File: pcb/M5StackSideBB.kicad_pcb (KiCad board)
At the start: 2 copper layers, 100 x 50 mm, 15 parts, among them J1 Conn_01x14, J2 Conn_01x14, J3 Conn_02x15_Odd_Even, J4 Conn_02x15_Odd_Even

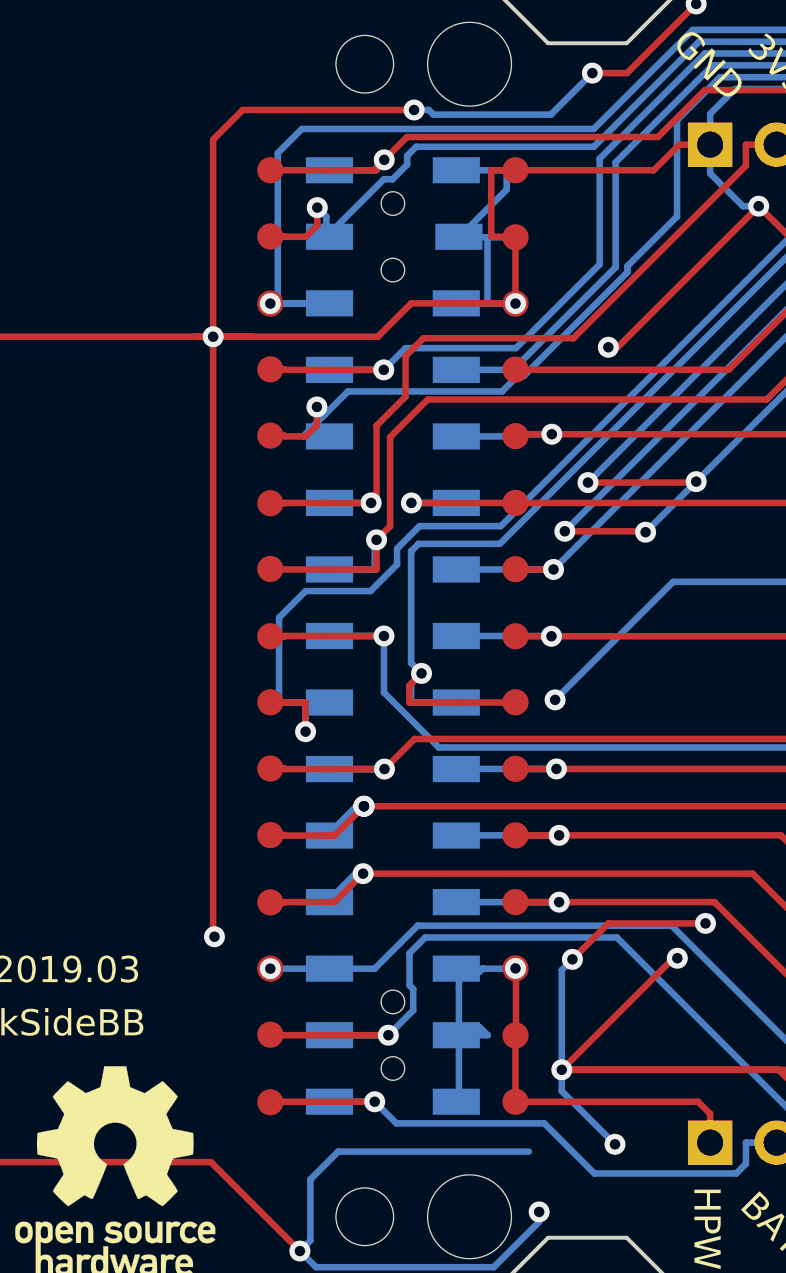
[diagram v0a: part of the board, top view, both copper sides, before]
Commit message: Add bottom pads for spacer PCB
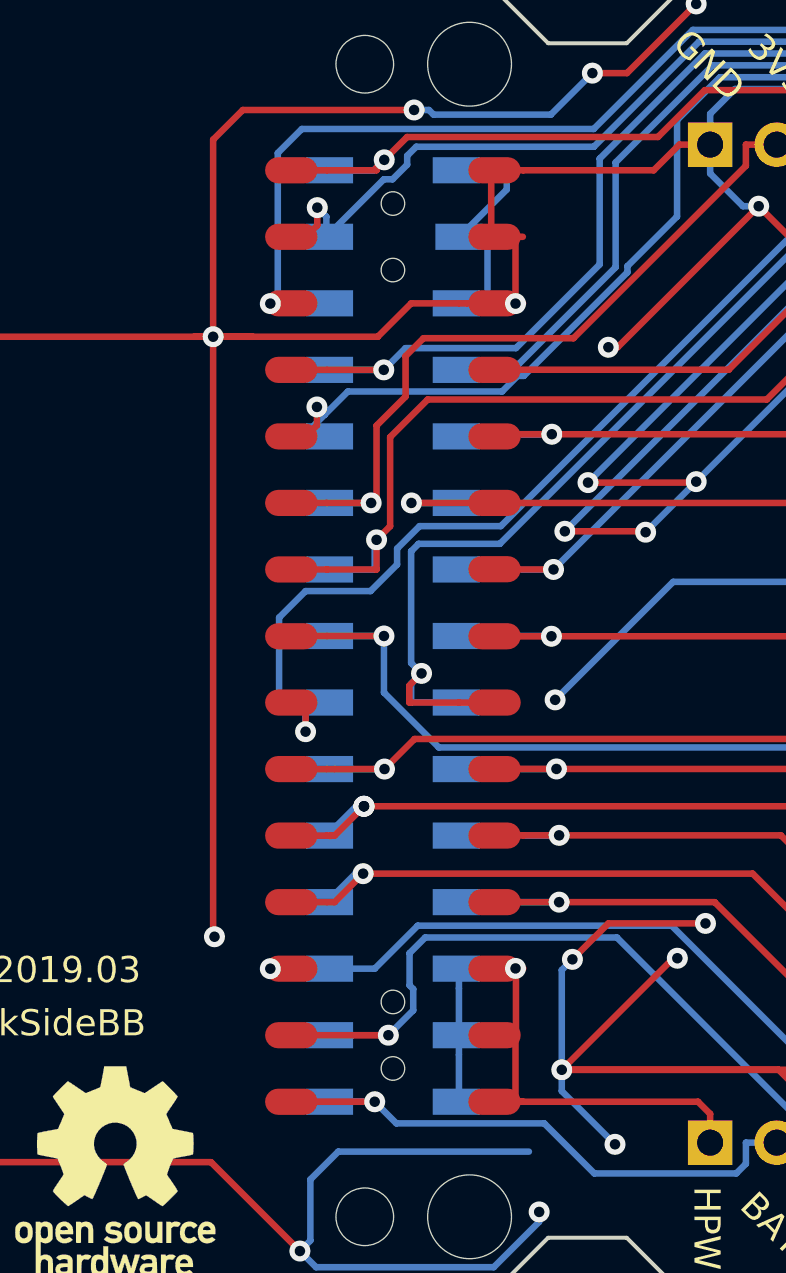
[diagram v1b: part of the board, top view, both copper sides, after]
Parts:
- J3: footprint footprints:PinHeader_2x15_P2.54mm_SMD_pads_only -> footprints:PinHeader_2x15_P2.54mm_M5Stack_SpacerPCB_pads
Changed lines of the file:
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@@
     (add_net RST)
   )
-  (module footprints:PinHeader_2x15_P2.54mm_SMD_pads_only (layer F.Cu)
+  (module footprints:PinHeader_2x15_P2.54mm_M5Stack_SpacerPCB_pads (layer F.Cu)
     (at 144.074 74.8284)
     (descr "surface-mounted straight pin header, 2x15, 2.54mm pitch, double rows")
@@
     (fp_line (start -1.59 -19.05) (end 2.54 -19.05) (layer F.Fab) (width 0.1))
     (fp_line (start 2.54 19.05) (end -2.54 19.05) (layer F.Fab) (width 0.1))
-    (pad "" np_thru_hole circle (at 0 13.97) (size 0.9 0.9) (drill 0.9) (layers *.Cu *.Mask))
-    (pad "" np_thru_hole circle (at 0 -13.97) (size 0.9 0.9) (drill 0.9) (layers *.Cu *.Mask))
-    (pad 30 smd circle (at 4.68 17.78) (size 1 1) (layers F.Cu F.Paste F.Mask)
+    (pad "" np_thru_hole oval (at 0 13.97) (size 0.9 0.9) (drill 0.9) (layers *.Cu *.Mask))
+    (pad "" np_thru_hole oval (at 0 -13.97) (size 0.9 0.9) (drill 0.9) (layers *.Cu *.Mask))
+    (pad 30 smd oval (at 3.88 17.78) (size 2 1) (layers F.Cu F.Paste F.Mask)
       (net 11 HPWR))
-    (pad 28 smd circle (at 4.68 15.25) (size 1 1) (layers F.Cu F.Paste F.Mask)
+    (pad 28 smd oval (at 3.88 15.24) (size 2 1) (layers F.Cu F.Paste F.Mask)
       (net 11 HPWR))
-    (pad 26 smd circle (at 4.68 12.69) (size 1 1) (layers F.Cu F.Paste F.Mask)
+    (pad 26 smd oval (at 3.88 12.7) (size 2 1) (layers F.Cu F.Paste F.Mask)
       (net 11 HPWR))
-    (pad 24 smd circle (at 4.68 10.16 90) (size 1 1) (layers F.Cu F.Paste F.Mask)
+    (pad 24 smd oval (at 3.88 10.16) (size 2 1) (layers F.Cu F.Paste F.Mask)
       (net 10 G15))
-    (pad 22 smd circle (at 4.68 7.61) (size 1 1) (layers F.Cu F.Paste F.Mask)
+    (pad 22 smd oval (at 3.88 7.62) (size 2 1) (layers F.Cu F.Paste F.Mask)
       (net 9 G12))
-    (pad 20 smd circle (at 4.68 5.07) (size 1 1) (layers F.Cu F.Paste F.Mask)
+    (pad 20 smd oval (at 3.88 5.08) (size 2 1) (layers F.Cu F.Paste F.Mask)
       (net 8 G2))
-    (pad 18 smd circle (at 4.68 2.53) (size 1 1) (layers F.Cu F.Paste F.Mask)
+    (pad 18 smd oval (at 3.88 2.54) (size 2 1) (layers F.Cu F.Paste F.Mask)
       (net 7 G21))
-    (pad 16 smd circle (at 4.68 0.01) (size 1 1) (layers F.Cu F.Paste F.Mask)
+    (pad 16 smd oval (at 3.88 0.01) (size 2 1) (layers F.Cu F.Paste F.Mask)
       (net 6 G16))
-    (pad 14 smd circle (at 4.68 -2.55) (size 1 1) (layers F.Cu F.Paste F.Mask)
+    (pad 14 smd oval (at 3.88 -2.55) (size 2 1) (layers F.Cu F.Paste F.Mask)
       (net 5 G3))
-    (pad 12 smd circle (at 4.68 -5.08) (size 1 1) (layers F.Cu F.Paste F.Mask)
+    (pad 12 smd oval (at 3.88 -5.08) (size 2 1) (layers F.Cu F.Paste F.Mask)
       (net 4 G18))
-    (pad 10 smd circle (at 4.68 -7.63) (size 1 1) (layers F.Cu F.Paste F.Mask)
+    (pad 10 smd oval (at 3.88 -7.62) (size 2 1) (layers F.Cu F.Paste F.Mask)
       (net 3 G19))
-    (pad 8 smd circle (at 4.68 -10.17) (size 1 1) (layers F.Cu F.Paste F.Mask)
+    (pad 8 smd oval (at 3.88 -10.16) (size 2 1) (layers F.Cu F.Paste F.Mask)
       (net 2 G23))
-    (pad 6 smd circle (at 4.68 -12.69) (size 1 1) (layers F.Cu F.Paste F.Mask)
+    (pad 6 smd oval (at 3.88 -12.7) (size 2 1) (layers F.Cu F.Paste F.Mask)
       (net 1 GND))
-    (pad 4 smd circle (at 4.68 -15.22) (size 1 1) (layers F.Cu F.Paste F.Mask)
+    (pad 4 smd oval (at 3.88 -15.24) (size 2 1) (layers F.Cu F.Paste F.Mask)
       (net 1 GND))
-    (pad 2 smd circle (at 4.68 -17.78) (size 1 1) (layers F.Cu F.Paste F.Mask)
+    (pad 2 smd oval (at 3.88 -17.78) (size 2 1) (layers F.Cu F.Paste F.Mask)
       (net 1 GND))
-    (pad 29 smd circle (at -4.68 17.8) (size 1 1) (layers F.Cu F.Paste F.Mask)
+    (pad 29 smd oval (at -3.88 17.78) (size 2 1) (layers F.Cu F.Paste F.Mask)
       (net 12 +BATT))
-    (pad 27 smd circle (at -4.68 15.22) (size 1 1) (layers F.Cu F.Paste F.Mask)
+    (pad 27 smd oval (at -3.88 15.24) (size 2 1) (layers F.Cu F.Paste F.Mask)
       (net 13 +5V))
-    (pad 25 smd circle (at -4.68 12.7) (size 1 1) (layers F.Cu F.Paste F.Mask)
+    (pad 25 smd oval (at -3.88 12.7) (size 2 1) (layers F.Cu F.Paste F.Mask)
       (net 14 G34))
-    (pad 23 smd circle (at -4.68 10.17) (size 1 1) (layers F.Cu F.Paste F.Mask)
+    (pad 23 smd oval (at -3.88 10.16) (size 2 1) (layers F.Cu F.Paste F.Mask)
       (net 15 G0))
-    (pad 21 smd circle (at -4.68 7.6) (size 1 1) (layers F.Cu F.Paste F.Mask)
+    (pad 21 smd oval (at -3.88 7.62) (size 2 1) (layers F.Cu F.Paste F.Mask)
       (net 16 G13))
-    (pad 19 smd circle (at -4.68 5.06) (size 1 1) (layers F.Cu F.Paste F.Mask)
+    (pad 19 smd oval (at -3.88 5.08) (size 2 1) (layers F.Cu F.Paste F.Mask)
       (net 17 G5))
-    (pad 17 smd circle (at -4.68 2.53) (size 1 1) (layers F.Cu F.Paste F.Mask)
+    (pad 17 smd oval (at -3.88 2.54) (size 2 1) (layers F.Cu F.Paste F.Mask)
       (net 18 G22))
-    (pad 15 smd circle (at -4.68 0.01) (size 1 1) (layers F.Cu F.Paste F.Mask)
+    (pad 15 smd oval (at -3.88 0.01) (size 2 1) (layers F.Cu F.Paste F.Mask)
       (net 19 G17))
-    (pad 13 smd circle (at -4.68 -2.56) (size 1 1) (layers F.Cu F.Paste F.Mask)
+    (pad 13 smd oval (at -3.88 -2.54) (size 2 1) (layers F.Cu F.Paste F.Mask)
       (net 20 G1))
-    (pad 11 smd circle (at -4.68 -5.07) (size 1 1) (layers F.Cu F.Paste F.Mask)
+    (pad 11 smd oval (at -3.88 -5.08) (size 2 1) (layers F.Cu F.Paste F.Mask)
       (net 26 +3V3))
-    (pad 9 smd circle (at -4.68 -7.65) (size 1 1) (layers F.Cu F.Paste F.Mask)
+    (pad 9 smd oval (at -3.88 -7.62) (size 2 1) (layers F.Cu F.Paste F.Mask)
       (net 21 G26))
-    (pad 7 smd circle (at -4.68 -10.18) (size 1 1) (layers F.Cu F.Paste F.Mask)
+    (pad 7 smd oval (at -3.88 -10.16) (size 2 1) (layers F.Cu F.Paste F.Mask)
       (net 22 G25))
-    (pad 5 smd circle (at -4.68 -12.69) (size 1 1) (layers F.Cu F.Paste F.Mask)
+    (pad 5 smd oval (at -3.88 -12.7) (size 2 1) (layers F.Cu F.Paste F.Mask)
       (net 23 RST))
-    (pad 3 smd circle (at -4.68 -15.25) (size 1 1) (layers F.Cu F.Paste F.Mask)
+    (pad 3 smd oval (at -3.88 -15.24) (size 2 1) (layers F.Cu F.Paste F.Mask)
       (net 24 G36))
-    (pad 1 smd circle (at -4.68 -17.78) (size 1 1) (layers F.Cu F.Paste F.Mask)
+    (pad 1 smd oval (at -3.88 -17.78) (size 2 1) (layers F.Cu F.Paste F.Mask)
       (net 25 G35))
     (model ${KISYS3DMOD}/Connector_PinHeader_2.54mm.3dshapes/PinHeader_2x15_P2.54mm_Vertical_SMD.wrl

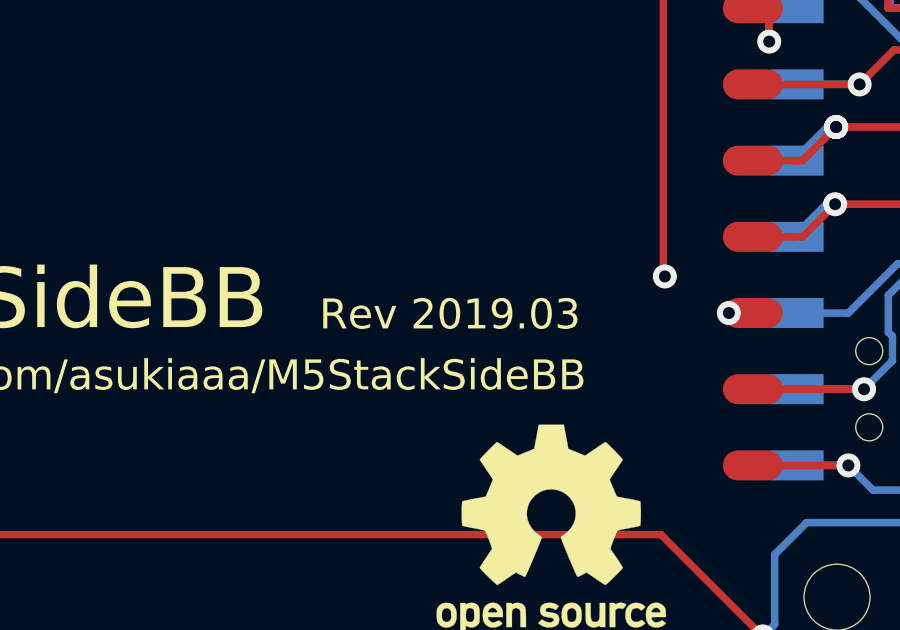
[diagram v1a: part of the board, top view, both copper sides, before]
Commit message: Update revision as 2019.05
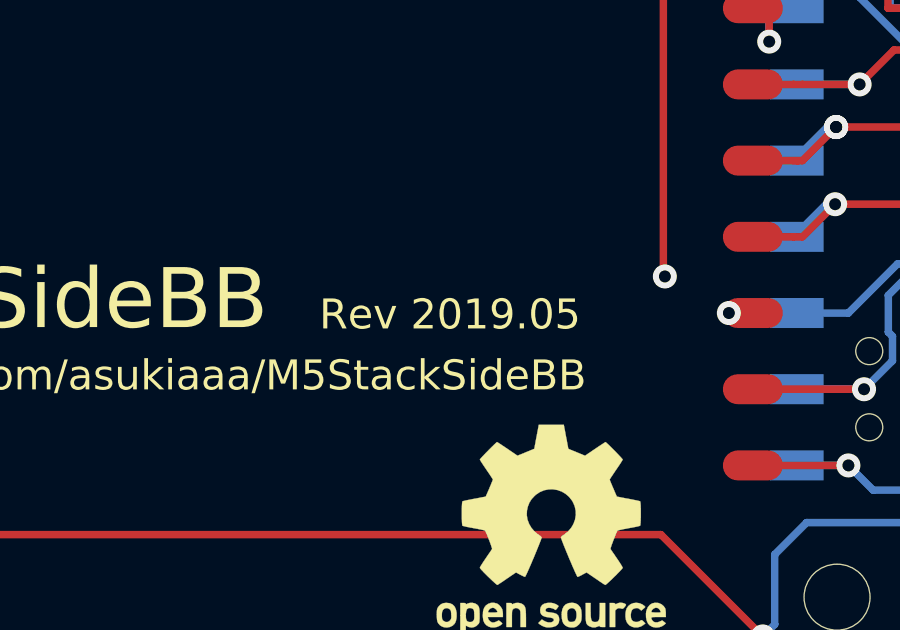
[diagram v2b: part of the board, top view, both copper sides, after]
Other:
- board text added: "Rev 2019.05"
- board text removed: "Rev 2019.03"
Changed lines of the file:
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@@
   (page A4)
   (layers
-    (0 F.Cu signal)
-    (31 B.Cu signal)
+    (0 F.Cu signal hide)
+    (31 B.Cu signal hide)
     (32 B.Adhes user)
     (33 F.Adhes user)
@@
     (effects (font (size 1 1) (thickness 0.25)))
   )
-  (gr_text "Rev 2019.03" (at 130.0988 87.5792) (layer F.SilkS)
+  (gr_text "Rev 2019.05" (at 130.0988 87.5792) (layer F.SilkS)
     (effects (font (size 1 1) (thickness 0.25)))
   )
@@
     (effects (font (size 1 1) (thickness 0.25)))
   )
-  (gr_text "Rev 2019.03" (at 160.74136 87.86876) (layer B.SilkS)
+  (gr_text "Rev 2019.05" (at 160.74136 87.86876) (layer B.SilkS)
     (effects (font (size 1.2 1.2) (thickness 0.3)) (justify mirror))
   )

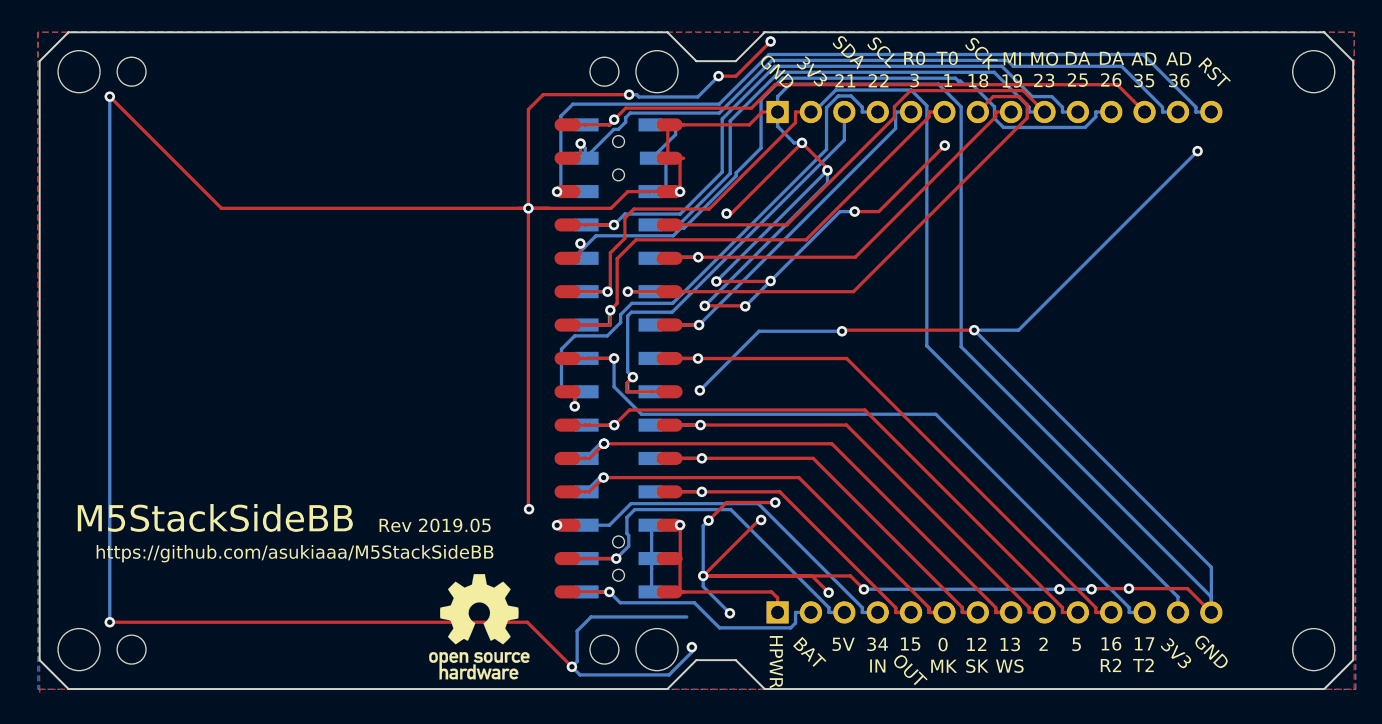
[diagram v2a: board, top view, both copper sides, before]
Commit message: Correct y center position for smd pads
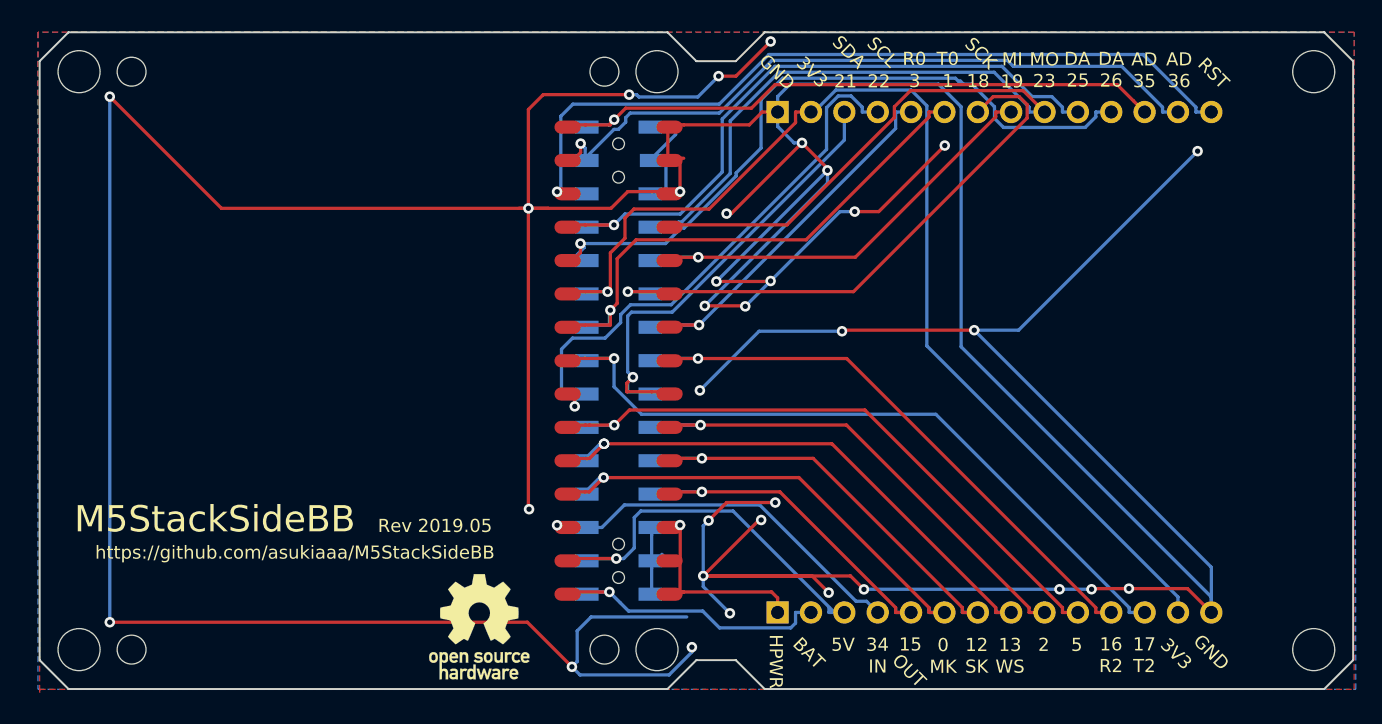
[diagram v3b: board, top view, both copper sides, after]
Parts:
- moved J3 0.17 mm to (144.1, 75.0)
- moved J4 0.17 mm to (144.1, 75.0)
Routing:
- net +5V: track 30.7 -> 31.8 mm

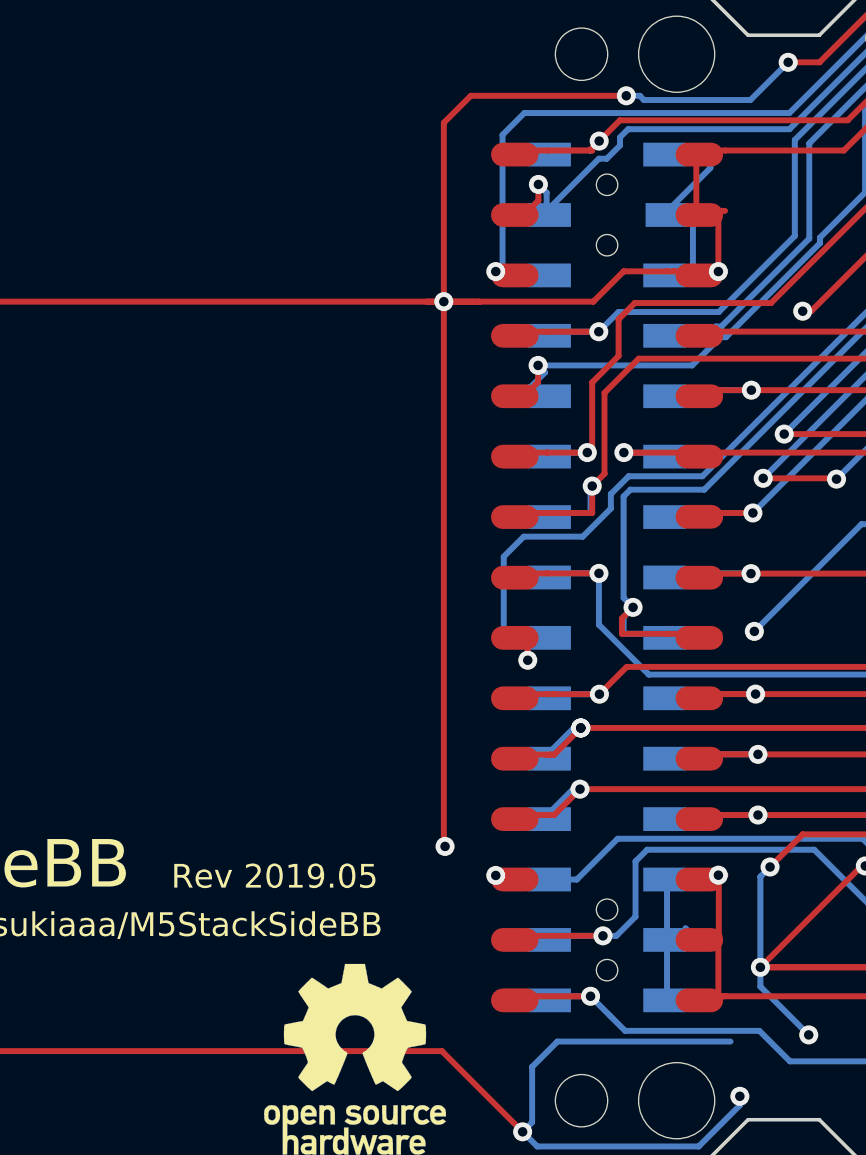
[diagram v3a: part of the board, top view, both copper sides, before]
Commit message: Update as narrow long style for pcb to spacer pads
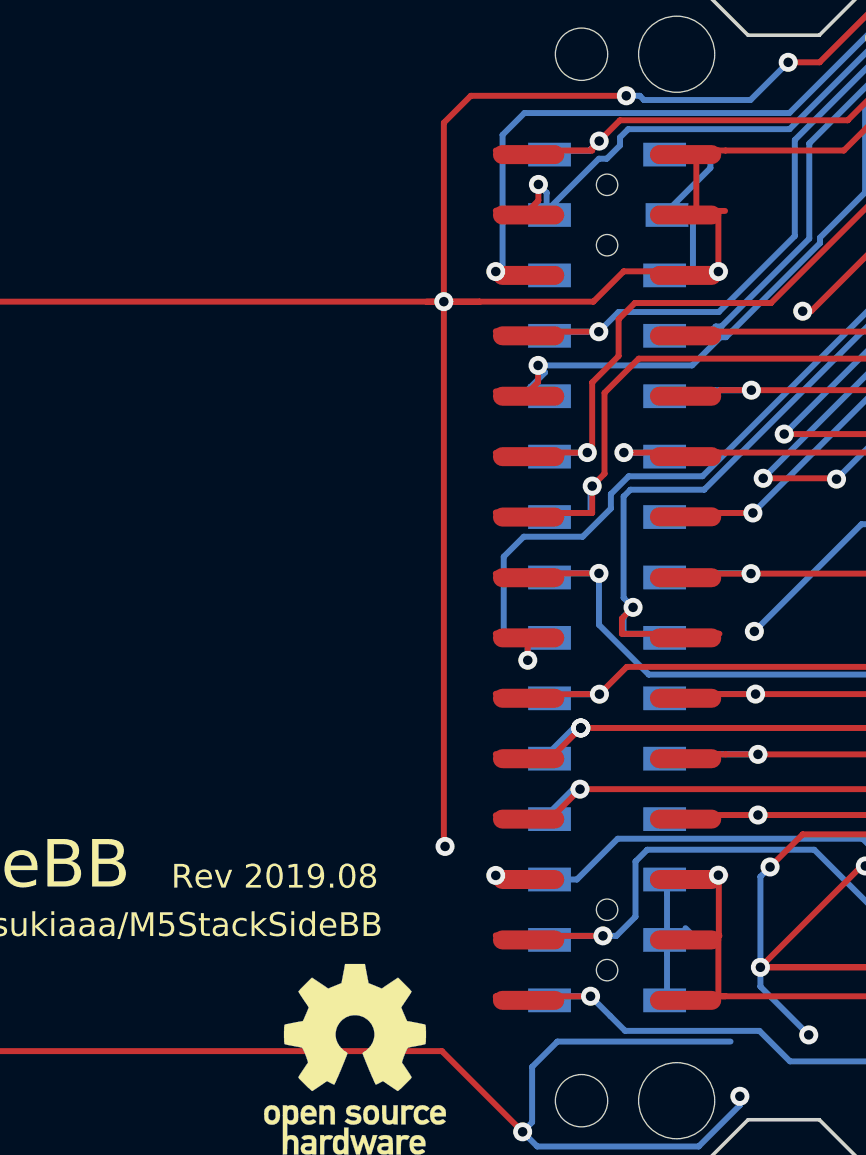
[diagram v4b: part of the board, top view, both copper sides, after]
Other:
- board text added: "Rev 2019.08"
- board text removed: "Rev 2019.05"
